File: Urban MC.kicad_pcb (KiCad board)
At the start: 2 copper layers, 33 parts, among them SW1 SW_Push, U1 IRS2186, U11 MCP2515-xSO, U12 TJA1050, U13 MCP4725xxx-xCH, U2 IRS2186, U3 IRS2186

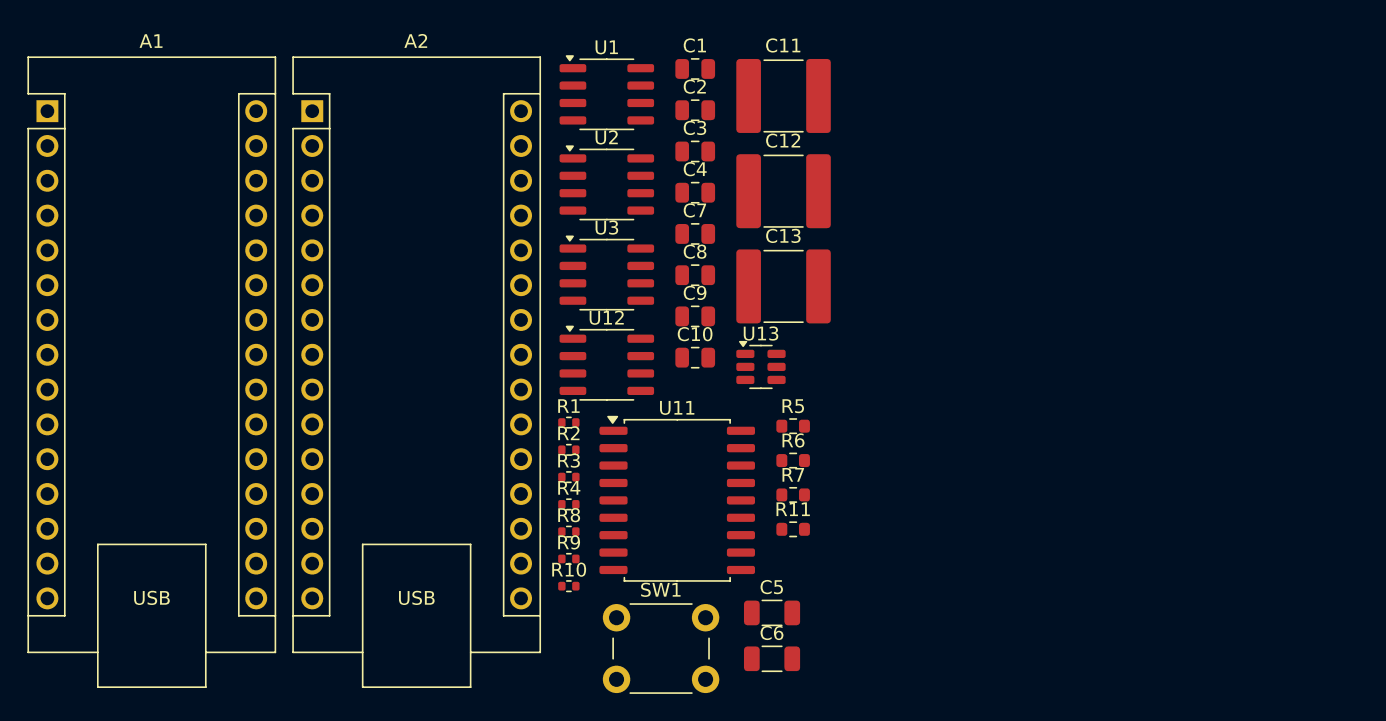
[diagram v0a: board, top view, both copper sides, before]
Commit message: added custom footprints
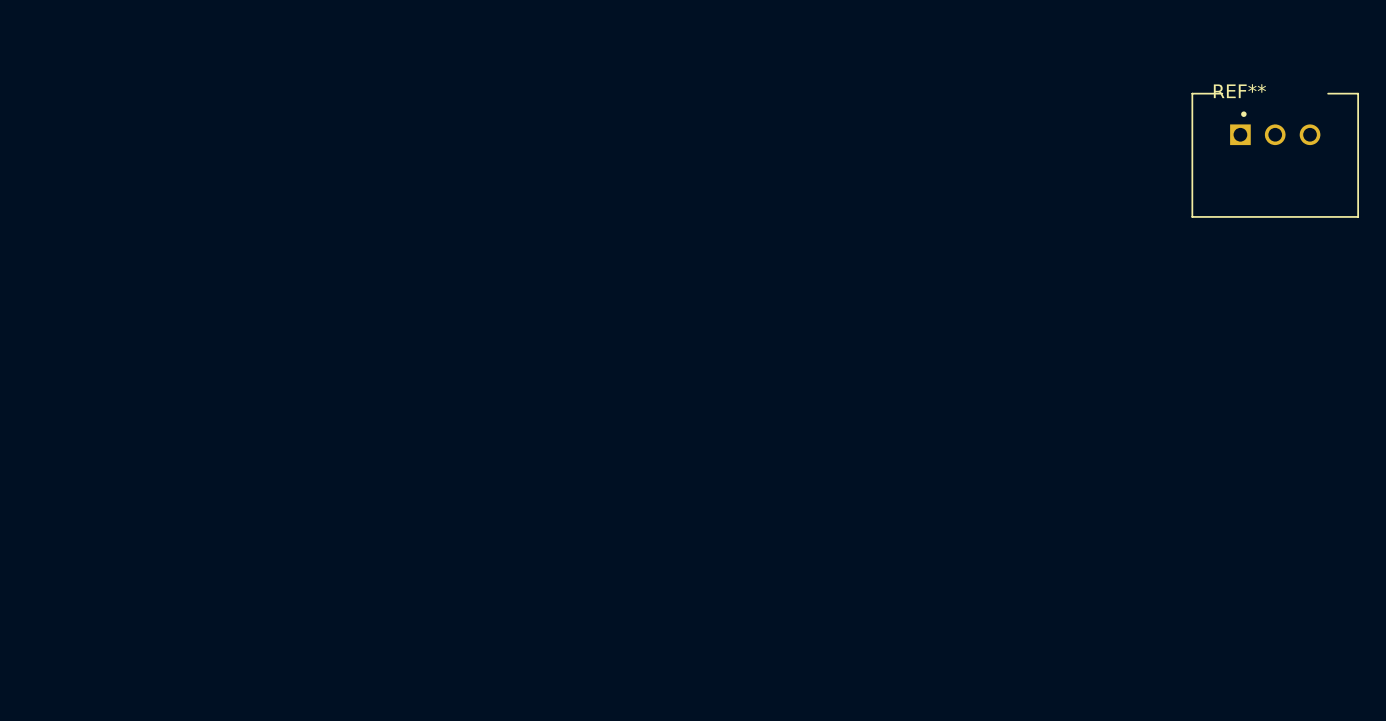
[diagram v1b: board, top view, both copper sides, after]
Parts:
- removed A1, A2: Arduino_Nano_v2.x, Module:Arduino_Nano
- removed C1, C10, C2, C3, C4, C7, C8, C9: 10u, Capacitor_SMD:C_0805_2012Metric
- removed C11, C12, C13: 1u, Capacitor_SMD:C_2220_5750Metric
- removed C5: 1u, Capacitor_SMD:C_1206_3216Metric
- removed C6: 22u, Capacitor_SMD:C_1206_3216Metric
- removed R1: 10K, Resistor_SMD:R_0402_1005Metric
- removed R10, R2, R3, R4, R8, R9: 11Ω, Resistor_SMD:R_0402_1005Metric
- removed R11: 120, Resistor_SMD:R_0603_1608Metric
- removed R5, R6, R7: 2.4Ω, Resistor_SMD:R_0603_1608Metric
- removed SW1: SW_Push, Button_Switch_THT:SW_PUSH_6mm
- removed U1, U2, U3: IRS2186, Package_SO:SOIC-8_3.9x4.9mm_P1.27mm
- removed U11: MCP2515-xSO, Package_SO:SOIC-18W_7.5x11.6mm_P1.27mm
- removed U12: TJA1050, Package_SO:SOIC-8_3.9x4.9mm_P1.27mm
- removed U13: MCP4725xxx-xCH, Package_TO_SOT_SMD:SOT-23-6
- added REF**: CONV_LCW78_12-1.0, urban_mc_custom_footprints:CONV_LCW78_12-1.0, F.Cu at (138.0, 62.5)

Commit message: updated schematic
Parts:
- removed REF**: CONV_LCW78_12-1.0, urban_mc_custom_footprints:CONV_LCW78_12-1.0
- added A1: Arduino_Nano_v2.x, Module:Arduino_Nano, F.Cu at (144.2, 42.2)
- added A2: Arduino_Nano_v2.x, Module:Arduino_Nano, F.Cu at (163.5, 42.2)
- added C1: 10u, Capacitor_SMD:C_0805_2012Metric, F.Cu at (172.1, 86.4)
- added C10: 10u, Capacitor_SMD:C_0805_2012Metric, F.Cu at (172.1, 107.5)
- added C11: 1u, Capacitor_SMD:C_2220_5750Metric, F.Cu at (178.6, 88.4)
- added C12: 1u, Capacitor_SMD:C_2220_5750Metric, F.Cu at (178.6, 95.4)
- added C13: 1u, Capacitor_SMD:C_2220_5750Metric, F.Cu at (178.6, 102.3)
- added C2: 10u, Capacitor_SMD:C_0805_2012Metric, F.Cu at (172.1, 89.5)
- added C3: 10u, Capacitor_SMD:C_0805_2012Metric, F.Cu at (172.1, 92.5)
- added C4: 10u, Capacitor_SMD:C_0805_2012Metric, F.Cu at (172.1, 95.5)
- added C5: 1u, Capacitor_SMD:C_1206_3216Metric, F.Cu at (188.5, 96.7)
- added C6: 22u, Capacitor_SMD:C_1206_3216Metric, F.Cu at (188.5, 100.0)
- added C7: 10u, Capacitor_SMD:C_0805_2012Metric, F.Cu at (172.1, 98.5)
- added C8: 10u, Capacitor_SMD:C_0805_2012Metric, F.Cu at (172.1, 101.5)
- added C9: 10u, Capacitor_SMD:C_0805_2012Metric, F.Cu at (172.1, 104.5)
- added D1: D, Diode_THT:D_DO-41_SOD81_P10.16mm_Horizontal, F.Cu at (182.7, 39.8)
- added D2: D, Diode_THT:D_DO-41_SOD81_P10.16mm_Horizontal, F.Cu at (182.7, 44.0)
- added HallConnectors1: Conn_01x03, urban_mc_custom_footprints:CON_436500300_MOL, F.Cu at (185.5, 108.6)
- added HallPowerInput1: Conn_01x02, urban_mc_custom_footprints:CON_436500200_MOL, F.Cu at (136.5, 40.5)
- added J1: Conn_01x02, urban_mc_custom_footprints:CON_436500200_MOL, F.Cu at (136.5, 54.0)
- added J10: Screw_Terminal_01x01, urban_mc_custom_footprints:WP-SHFU_7461100, F.Cu at (119.5, 117.3)
- added J2: Conn_01x02, urban_mc_custom_footprints:CON_436500200_MOL, F.Cu at (136.5, 67.6)
- added J3: Screw_Terminal_01x02, urban_mc_custom_footprints:CON_436500200_MOL, F.Cu at (136.5, 81.2)
- added J6: Screw_Terminal_01x01, urban_mc_custom_footprints:WP-SHFU_7461100, F.Cu at (119.5, 46.5)
- added J7: Screw_Terminal_01x01, urban_mc_custom_footprints:WP-SHFU_7461100, F.Cu at (119.5, 64.2)
- added J8: Screw_Terminal_01x01, urban_mc_custom_footprints:WP-SHFU_7461100, F.Cu at (119.5, 81.9)
- added J9: Screw_Terminal_01x01, urban_mc_custom_footprints:WP-SHFU_7461100, F.Cu at (119.5, 99.6)
- added R1: 10K, Resistor_SMD:R_0402_1005Metric, F.Cu at (184.2, 85.9)
- added R10: 11Ω, Resistor_SMD:R_0402_1005Metric, F.Cu at (184.2, 97.9)
- added R11: 120, Resistor_SMD:R_0603_1608Metric, F.Cu at (187.7, 93.7)
- added R2: 11Ω, Resistor_SMD:R_0402_1005Metric, F.Cu at (184.2, 87.9)
- added R3: 11Ω, Resistor_SMD:R_0402_1005Metric, F.Cu at (184.2, 89.9)
- added R4: 11Ω, Resistor_SMD:R_0402_1005Metric, F.Cu at (184.2, 91.9)
- added R5: 2.4Ω, Resistor_SMD:R_0603_1608Metric, F.Cu at (187.7, 86.2)
- added R6: 2.4Ω, Resistor_SMD:R_0603_1608Metric, F.Cu at (187.7, 88.7)
- added R7: 2.4Ω, Resistor_SMD:R_0603_1608Metric, F.Cu at (187.7, 91.2)
- added R8: 11Ω, Resistor_SMD:R_0402_1005Metric, F.Cu at (184.2, 93.9)
- added R9: 11Ω, Resistor_SMD:R_0402_1005Metric, F.Cu at (184.2, 95.9)
- added SW1: SW_Push, Button_Switch_THT:SW_PUSH_6mm, F.Cu at (182.8, 72.0)
- added U1: IRS2186, Package_SO:SOIC-8_3.9x4.9mm_P1.27mm, F.Cu at (165.7, 88.3)
- added U10: ~, urban_mc_custom_footprints:CONV_LCW78_12-1.0, F.Cu at (187.9, 52.2)
- added U11: MCP2515-xSO, Package_SO:SOIC-18W_7.5x11.6mm_P1.27mm, F.Cu at (187.2, 63.4)
- added U12: TJA1050, Package_SO:SOIC-8_3.9x4.9mm_P1.27mm, F.Cu at (165.7, 108.0)
- added U13: MCP4725, Package_TO_SOT_SMD:SOT-23-6, F.Cu at (183.4, 80.9)
- added U2: IRS2186, Package_SO:SOIC-8_3.9x4.9mm_P1.27mm, F.Cu at (165.7, 94.9)
- added U3: IRS2186, Package_SO:SOIC-8_3.9x4.9mm_P1.27mm, F.Cu at (165.7, 101.5)
- added U4: IRF150P220XKMA1, urban_mc_custom_footprints:PG-TO247-3-901_INF, F.Cu at (147.2, 88.4)
- added U5: IRF150P220XKMA1, urban_mc_custom_footprints:PG-TO247-3-901_INF, F.Cu at (147.2, 95.4)
- added U6: IRF150P220XKMA1, urban_mc_custom_footprints:PG-TO247-3-901_INF, F.Cu at (147.2, 102.4)
- added U7: IRF150P220XKMA1, urban_mc_custom_footprints:PG-TO247-3-901_INF, F.Cu at (147.2, 109.3)
- added U8: IRF150P220XKMA1, urban_mc_custom_footprints:PG-TO247-3-901_INF, F.Cu at (147.2, 116.3)
- added U9: IRF150P220XKMA1, urban_mc_custom_footprints:PG-TO247-3-901_INF, F.Cu at (147.2, 123.3)

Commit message: Updated mosfet symbol
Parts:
- removed J10, J9: Screw_Terminal_01x01, urban_mc_custom_footprints:WP-SHFU_7461100
- removed U4, U5, U6, U7, U8, U9: IRF150P220XKMA1, urban_mc_custom_footprints:PG-TO247-3-901_INF
- added D3: D, Diode_THT:D_DO-41_SOD81_P10.16mm_Horizontal, F.Cu at (173.8, 1.75)
- added D4: D, Diode_THT:D_DO-41_SOD81_P10.16mm_Horizontal, F.Cu at (173.8, 6.00)
- added J4: Screw_Terminal_01x01, urban_mc_custom_footprints:WP-SHFU_7461100, F.Cu at (113.3, -58.2)
- added J5: Screw_Terminal_01x01, urban_mc_custom_footprints:WP-SHFU_7461100, F.Cu at (133.7, -58.8)
- added Q1: IQE022N06LM5CGSCATMA1, urban_mc_custom_footprints:IFX-PG-WHTFN-9-1-V, F.Cu at (146.1, -22.7)
- added Q10: IQE022N06LM5CGSCATMA1, urban_mc_custom_footprints:IFX-PG-WHTFN-9-1-V, F.Cu at (152.2, -11.3)
- added Q11: IQE022N06LM5CGSCATMA1, urban_mc_custom_footprints:IFX-PG-WHTFN-9-1-V, F.Cu at (152.2, -5.58)
- added Q12: IQE022N06LM5CGSCATMA1, urban_mc_custom_footprints:IFX-PG-WHTFN-9-1-V, F.Cu at (152.2, 0.14)
- added Q13: IQE022N06LM5CGSCATMA1, urban_mc_custom_footprints:IFX-PG-WHTFN-9-1-V, F.Cu at (152.2, 5.85)
- added Q14: IQE022N06LM5CGSCATMA1, urban_mc_custom_footprints:IFX-PG-WHTFN-9-1-V, F.Cu at (152.2, 11.6)
- added Q15: IQE022N06LM5CGSCATMA1, urban_mc_custom_footprints:IFX-PG-WHTFN-9-1-V, F.Cu at (158.4, -22.7)
- added Q16: IQE022N06LM5CGSCATMA1, urban_mc_custom_footprints:IFX-PG-WHTFN-9-1-V, F.Cu at (158.4, -17.0)
- added Q17: IQE022N06LM5CGSCATMA1, urban_mc_custom_footprints:IFX-PG-WHTFN-9-1-V, F.Cu at (158.4, -11.3)
- added Q18: IQE022N06LM5CGSCATMA1, urban_mc_custom_footprints:IFX-PG-WHTFN-9-1-V, F.Cu at (158.4, -5.58)
- added Q19: IQE022N06LM5CGSCATMA1, urban_mc_custom_footprints:IFX-PG-WHTFN-9-1-V, F.Cu at (158.4, 0.14)
- added Q2: IQE022N06LM5CGSCATMA1, urban_mc_custom_footprints:IFX-PG-WHTFN-9-1-V, F.Cu at (146.1, -17.0)
- added Q20: IQE022N06LM5CGSCATMA1, urban_mc_custom_footprints:IFX-PG-WHTFN-9-1-V, F.Cu at (158.4, 5.85)
- added Q21: IQE022N06LM5CGSCATMA1, urban_mc_custom_footprints:IFX-PG-WHTFN-9-1-V, F.Cu at (158.4, 11.6)
- added Q22: IQE022N06LM5CGSCATMA1, urban_mc_custom_footprints:IFX-PG-WHTFN-9-1-V, F.Cu at (164.5, -22.7)
- added Q23: IQE022N06LM5CGSCATMA1, urban_mc_custom_footprints:IFX-PG-WHTFN-9-1-V, F.Cu at (164.5, -17.0)
- added Q24: IQE022N06LM5CGSCATMA1, urban_mc_custom_footprints:IFX-PG-WHTFN-9-1-V, F.Cu at (164.5, -11.3)
- added Q3: IQE022N06LM5CGSCATMA1, urban_mc_custom_footprints:IFX-PG-WHTFN-9-1-V, F.Cu at (146.1, -11.3)
- added Q4: IQE022N06LM5CGSCATMA1, urban_mc_custom_footprints:IFX-PG-WHTFN-9-1-V, F.Cu at (146.1, -5.58)
- added Q5: IQE022N06LM5CGSCATMA1, urban_mc_custom_footprints:IFX-PG-WHTFN-9-1-V, F.Cu at (146.1, 0.14)
- added Q6: IQE022N06LM5CGSCATMA1, urban_mc_custom_footprints:IFX-PG-WHTFN-9-1-V, F.Cu at (146.1, 5.85)
- added Q7: IQE022N06LM5CGSCATMA1, urban_mc_custom_footprints:IFX-PG-WHTFN-9-1-V, F.Cu at (146.1, 11.6)
- added Q8: IQE022N06LM5CGSCATMA1, urban_mc_custom_footprints:IFX-PG-WHTFN-9-1-V, F.Cu at (152.2, -22.7)
- added Q9: IQE022N06LM5CGSCATMA1, urban_mc_custom_footprints:IFX-PG-WHTFN-9-1-V, F.Cu at (152.2, -17.0)
- C11, C13: value 1u -> 10u; footprint Capacitor_SMD:C_2220_5750Metric -> Capacitor_SMD:C_0805_2012Metric
- C2: value 10u -> 1u; footprint Capacitor_SMD:C_0805_2012Metric -> Capacitor_SMD:C_1206_3216Metric
- C3: value 10u -> 22u; footprint Capacitor_SMD:C_0805_2012Metric -> Capacitor_SMD:C_1206_3216Metric
- C5: value 1u -> 10u; footprint Capacitor_SMD:C_1206_3216Metric -> Capacitor_SMD:C_0805_2012Metric
- C6: value 22u -> 1u; footprint Capacitor_SMD:C_1206_3216Metric -> Capacitor_SMD:C_2220_5750Metric
- C9: value 10u -> 1u; footprint Capacitor_SMD:C_0805_2012Metric -> Capacitor_SMD:C_2220_5750Metric
- R10, R3: value 11Ω -> 2.4Ω; footprint Resistor_SMD:R_0402_1005Metric -> Resistor_SMD:R_0603_1608Metric
- R5, R6: value 2.4Ω -> 11Ω; footprint Resistor_SMD:R_0603_1608Metric -> Resistor_SMD:R_0402_1005Metric
- moved R11 174.1 mm to (23.8, 152.5)
- moved C1 166.4 mm to (95.1, -61.0)
- moved C2 163.7 mm to (96.0, -55.5)
- moved C3 163.4 mm to (96.0, -52.2)
- moved J1 162.8 mm to (21.3, 169.2)
- moved R1 158.9 mm to (65.0, -19.0), turned to 180 degrees
- moved J6 154.5 mm to (251.2, 127.2), turned to 90 degrees
- moved U10 152.9 mm to (83.8, -59.8), turned to 180 degrees
- moved C13 151.8 mm to (99.1, -27.0)
- moved HallConnectors1 149.0 mm to (100.1, -13.5), turned to 90 degrees
- moved U11 147.0 mm to (41.7, 42.9)
- moved U13 145.1 mm to (73.6, -14.0)
- moved D1 143.2 mm to (88.4, -68.0)
- moved J7 135.9 mm to (249.8, 102.7), turned to 90 degrees
- moved A2 134.0 mm to (34.8, 79.4)
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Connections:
- C1 pad 1: Net-(U1-VS) -> +48V
- C1 pad 2: Net-(D2-K) -> GND
- C11 pad 1: +48V -> Net-(U3-VS)
- C11 pad 2: GND -> Net-(D4-K)
- C12 pad 1: +48V -> GND
- C12 pad 2: GND -> Net-(J6-Pin_1)
- C13 pad 1: +48V -> +5V
- C2 pad 1: Net-(U2-VS) -> +48V
- C2 pad 2: Net-(U2-VB) -> GND
- C3 pad 1: Net-(U3-VS) -> +12V
- C3 pad 2: Net-(U3-VB) -> GND
- C4 pad 1: +48V -> GND
- C4 pad 2: GND -> +12V
- C5 pad 1: +48V -> Net-(U1-VS)
- C5 pad 2: GND -> Net-(D2-K)
- C6 pad 1: +12V -> GND
- C6 pad 2: GND -> Net-(J8-Pin_1)
- C7 pad 1: +5V -> GND
- C7 pad 2: GND -> +12V
- C8 pad 1: GND -> Net-(U2-VS)
- C8 pad 2: +12V -> Net-(D3-K)
- C9 pad 2: +12V -> Net-(J7-Pin_1)
- R10 pad 1: Net-(U3-HO) -> Net-(U3-VS)
- R10 pad 2: Net-(U8-GATE) -> Net-(J6-Pin_1)
- R2 pad 1: Net-(U1-LO) -> Net-(U1-HO)
- R3 pad 1: Net-(U2-LO) -> Net-(U1-VS)
- R3 pad 2: Net-(U7-GATE) -> Net-(J8-Pin_1)
- R4 pad 1: Net-(U3-LO) -> Net-(U1-LO)
- R5 pad 1: Net-(U1-VS) -> Net-(U2-LO)
- R5 pad 2: Net-(J6-Pin_1) -> Net-(Q10-GATE)
- R6 pad 1: Net-(U2-VS) -> Net-(U2-HO)
- R6 pad 2: Net-(J7-Pin_1) -> Net-(Q11-GATE)
- R7 pad 1: Net-(U3-VS) -> Net-(U2-VS)
- R7 pad 2: Net-(J8-Pin_1) -> Net-(J7-Pin_1)
- R8 pad 1: Net-(U2-HO) -> Net-(U3-LO)
- R9 pad 1: Net-(U1-HO) -> Net-(U3-HO)
- U1 pad 1: Net-(A1-D6) -> Net-(A1-D10)
- U1 pad 2: Net-(A1-D9) -> Net-(A1-D11)
- U2 pad 8: Net-(U2-VB) -> Net-(D3-K)
- U3 pad 1: Net-(A1-D10) -> Net-(A1-D6)
- U3 pad 2: Net-(A1-D11) -> Net-(A1-D9)
- U3 pad 8: Net-(U3-VB) -> Net-(D4-K)
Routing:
- added copper zone on F.Cu, net +12V
- added copper zone on B.Cu, net +48V
- added copper zone on In1.Cu, net GND
- added copper zone on In2.Cu, net GND
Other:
- board outline added: 167 x 104 mm
- copper layers 2 -> 4

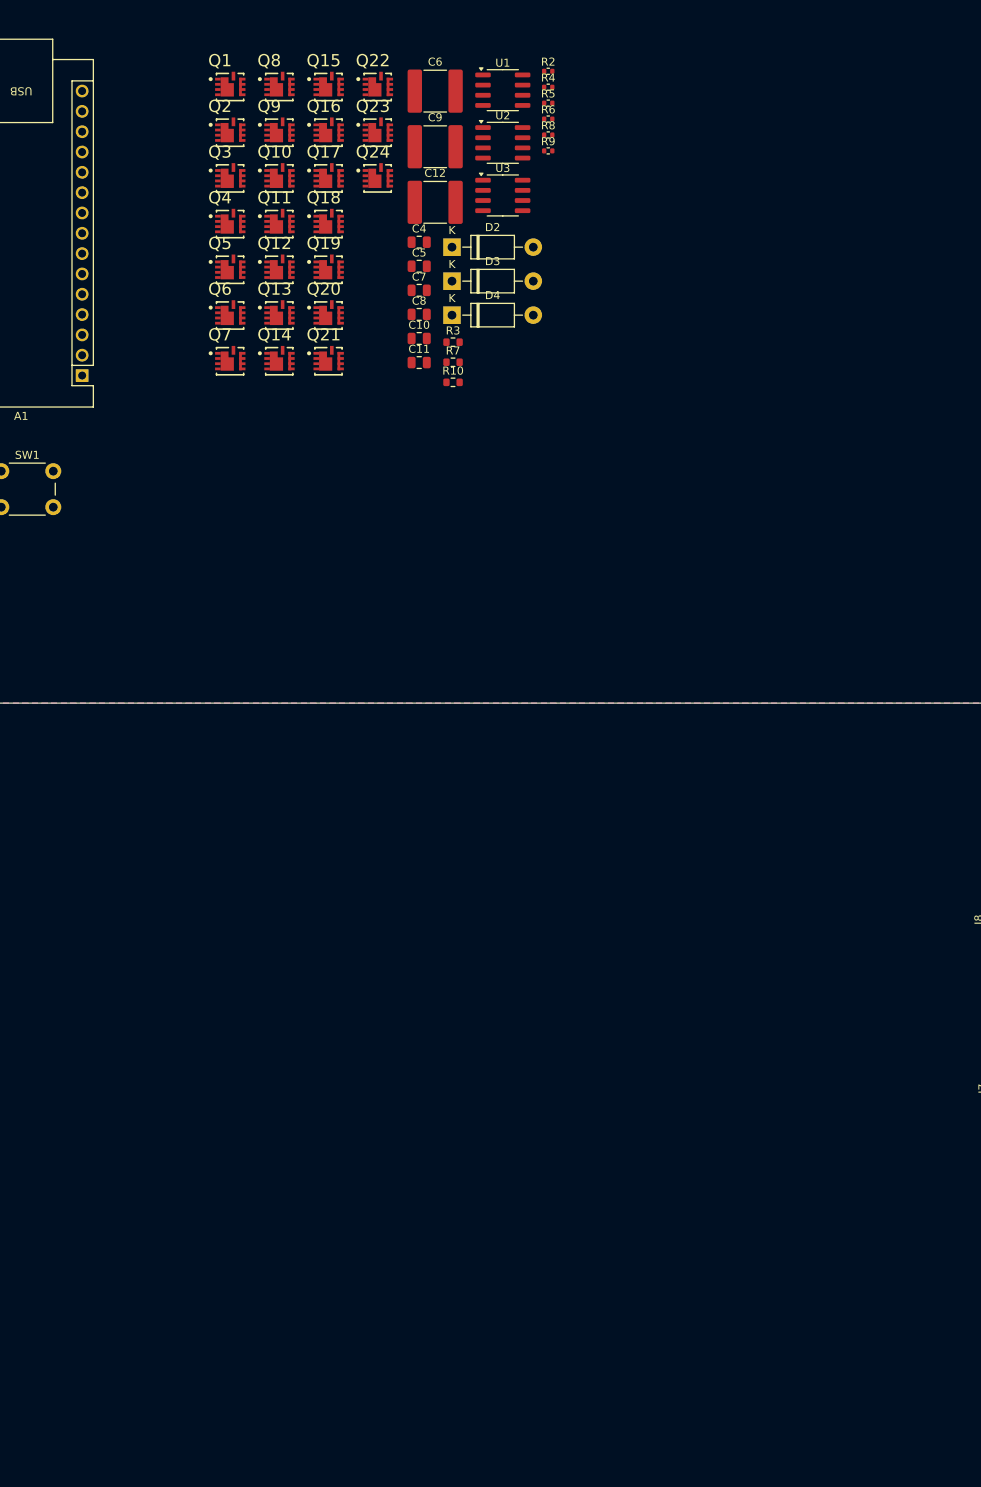
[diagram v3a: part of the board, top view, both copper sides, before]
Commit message: Updated layout
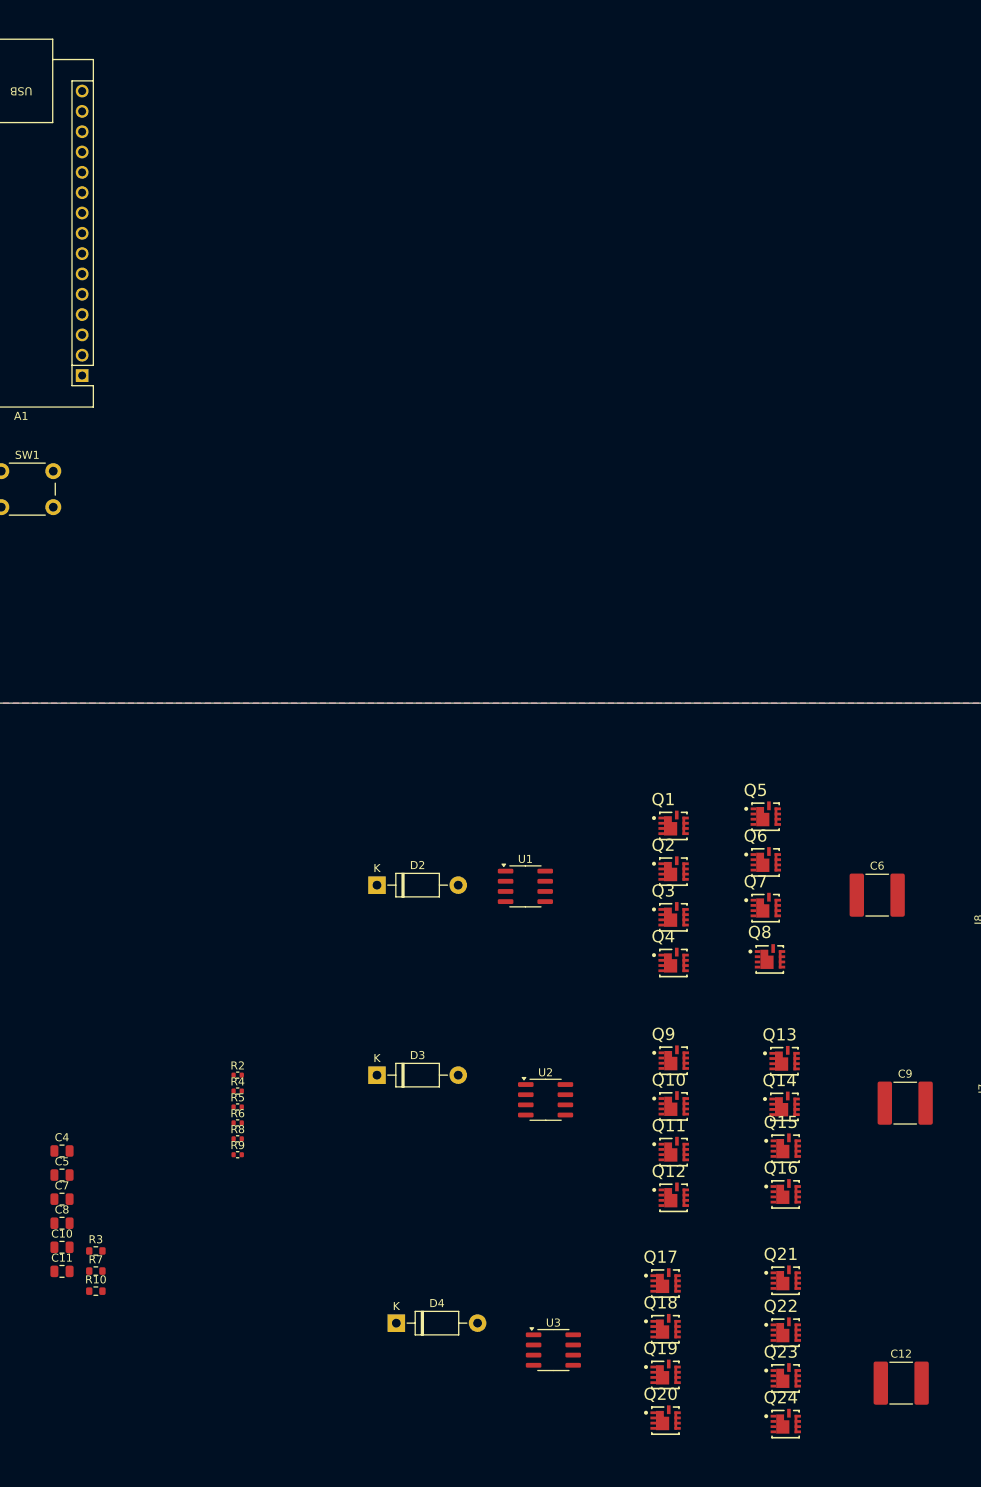
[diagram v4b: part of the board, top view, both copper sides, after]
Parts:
- moved Q22 163.8 mm to (215.5, 133.0)
- moved Q23 163.8 mm to (215.5, 138.7)
- moved Q24 163.8 mm to (215.5, 144.4)
- moved C12 158.7 mm to (229.9, 139.5)
- moved Q15 144.5 mm to (215.5, 110.0)
- moved Q16 144.5 mm to (215.5, 115.7)
- moved U3 144.5 mm to (186.5, 135.4)
- moved Q17 144.4 mm to (200.5, 126.9)
- moved Q18 144.4 mm to (200.5, 132.6)
- moved Q19 144.4 mm to (200.5, 138.3)
- moved Q20 144.4 mm to (200.5, 144.0)
- moved C9 133.2 mm to (230.4, 104.5)
- moved R2 131.3 mm to (147.0, 101.0)
- moved R5 131.3 mm to (147.0, 105.0)
- moved R6 131.3 mm to (147.0, 107.0)
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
